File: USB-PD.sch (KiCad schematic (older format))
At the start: 54 parts, among them IC3 TPS7A0518PDBVT, J1 1053131102, J11 E8124-015-01, Q10 Si7223DN, Q11 Si7223DN, Q9 SQS401EN-T1_BE3, U12 STUSB4500QTR, U14 LTC4418IUF#PBF

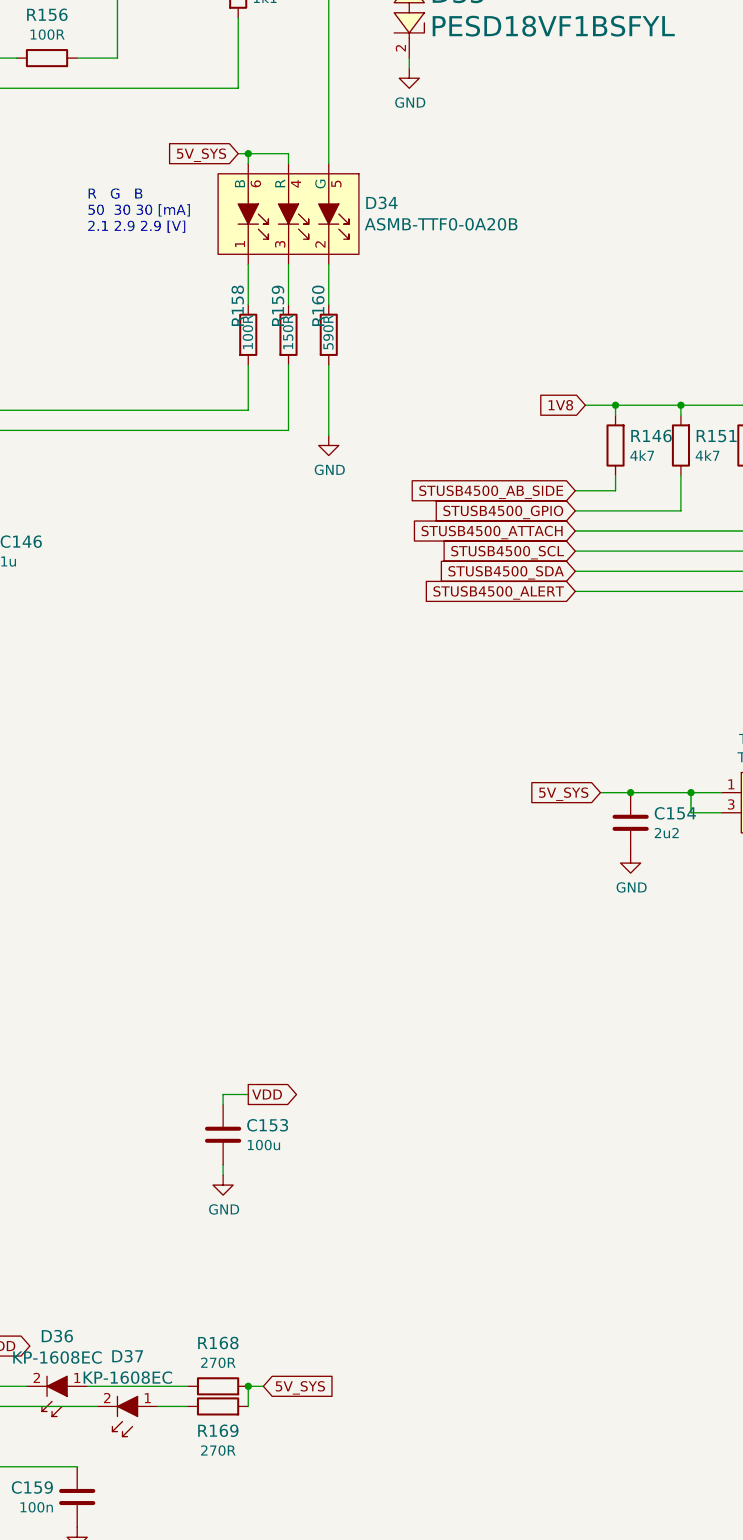
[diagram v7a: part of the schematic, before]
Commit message: Connecting LT9611
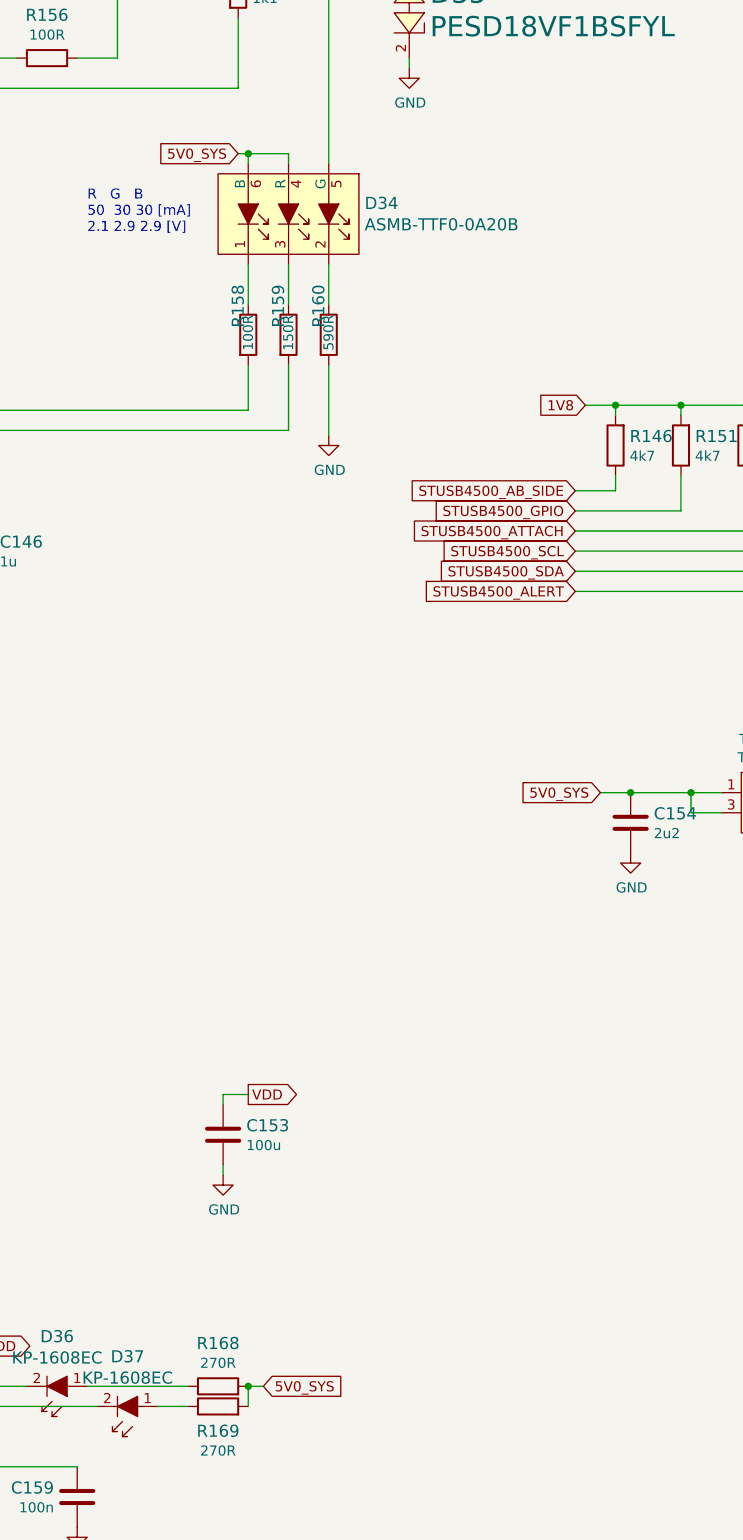
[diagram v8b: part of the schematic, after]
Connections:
- net 5V_SYS renamed 5V0_SYS
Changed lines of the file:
@@
 $EndComp
 Text GLabel 10600 2075 0    50   Input ~ 0
-5V_SYS
+5V0_SYS
 Text Notes 9850 2475 0    50   ~ 0
 R   G   B\n50  30 30 [mA]\n2.1 2.9 2.9 [V]
@@
 1V8
 Text GLabel 12400 5250 0    50   Input ~ 0
-5V_SYS
+5V0_SYS
 $Comp
 L sc606-baseboard:1053131102 J1
@@
 	9325 8200 9550 8200
 Text GLabel 10725 8200 2    50   Input ~ 0
-5V_SYS
+5V0_SYS
 Wire Wire Line
 	10650 8200 10650 8300
